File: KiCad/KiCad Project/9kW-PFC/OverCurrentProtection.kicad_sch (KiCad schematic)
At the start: 0 parts

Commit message: Added submodule for KiCad Library
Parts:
- added U1: MCP6004, Package_SO:SOIC-14_3.9x8.7mm_P1.27mm, symbol Amplifier_Operational:MCP6004

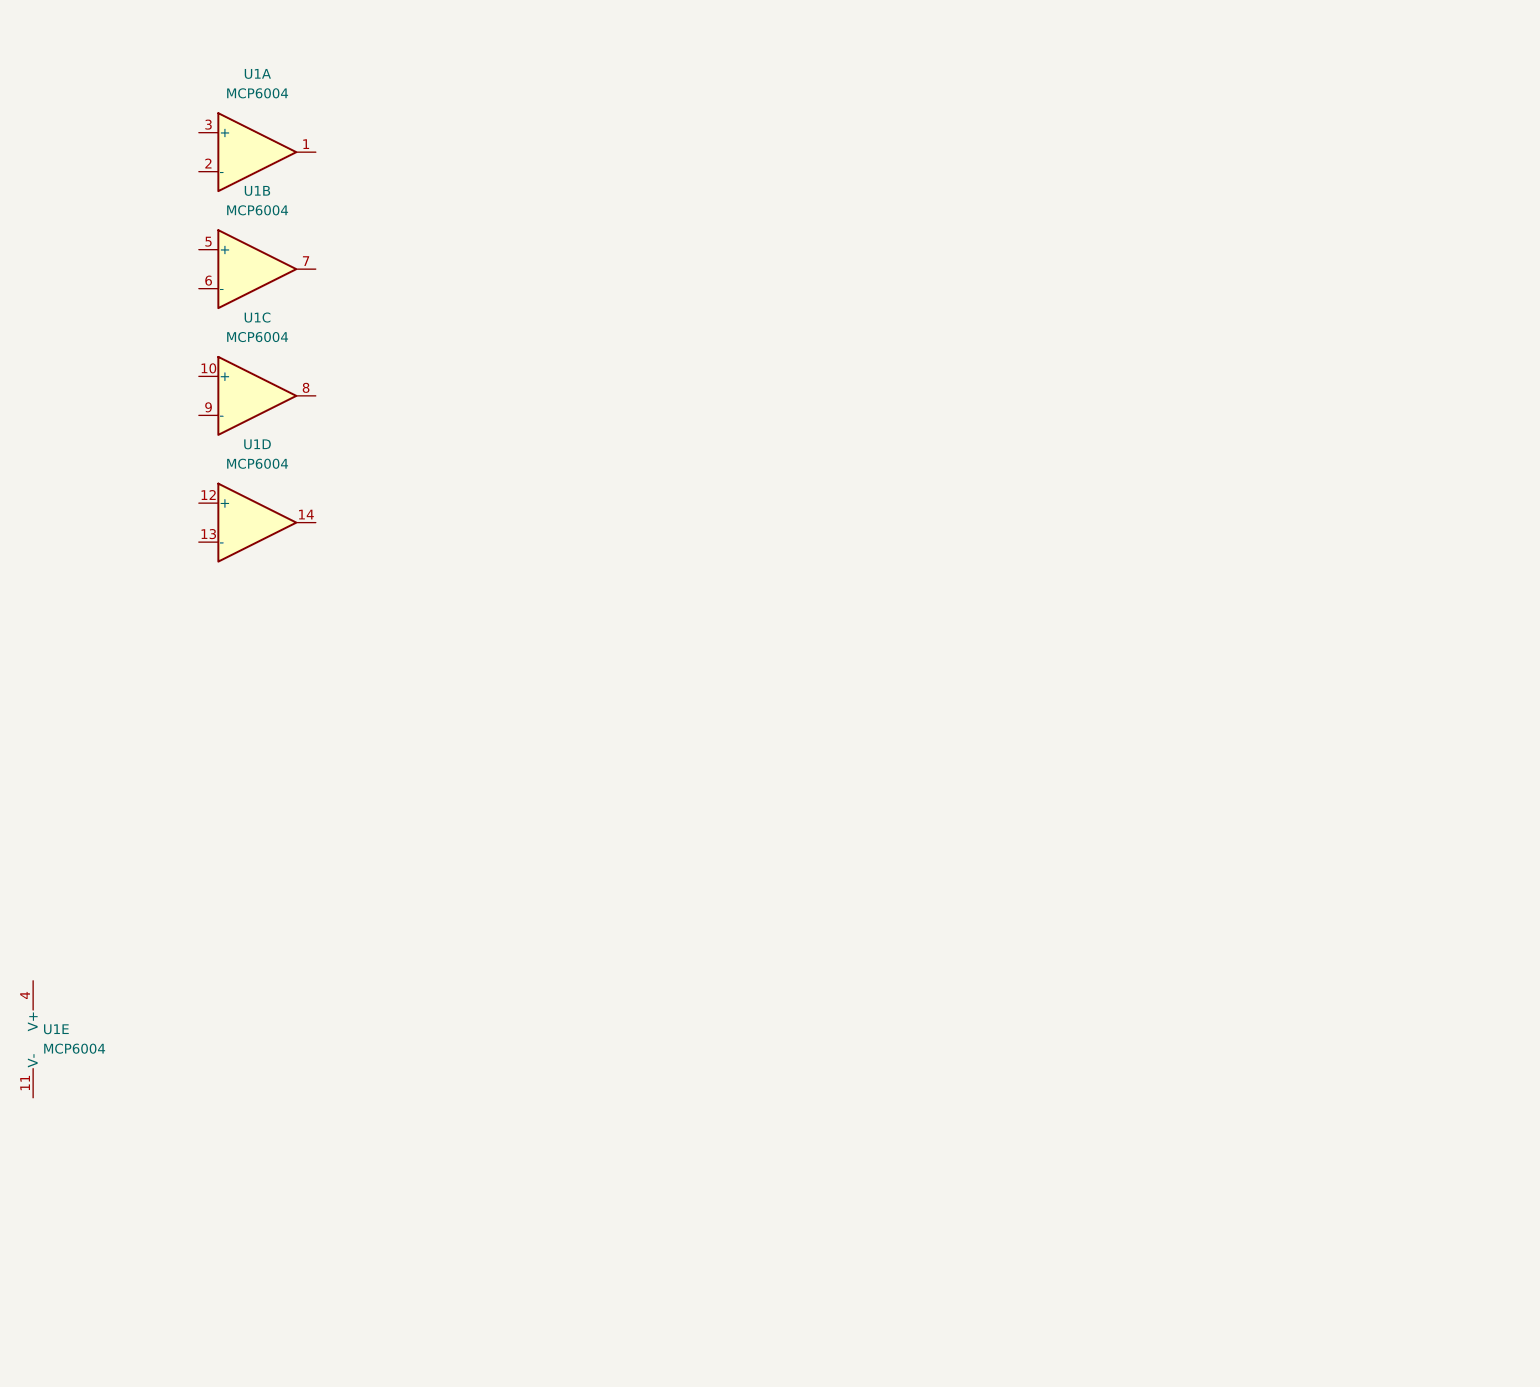
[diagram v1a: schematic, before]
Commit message: Started on Over Current Protection
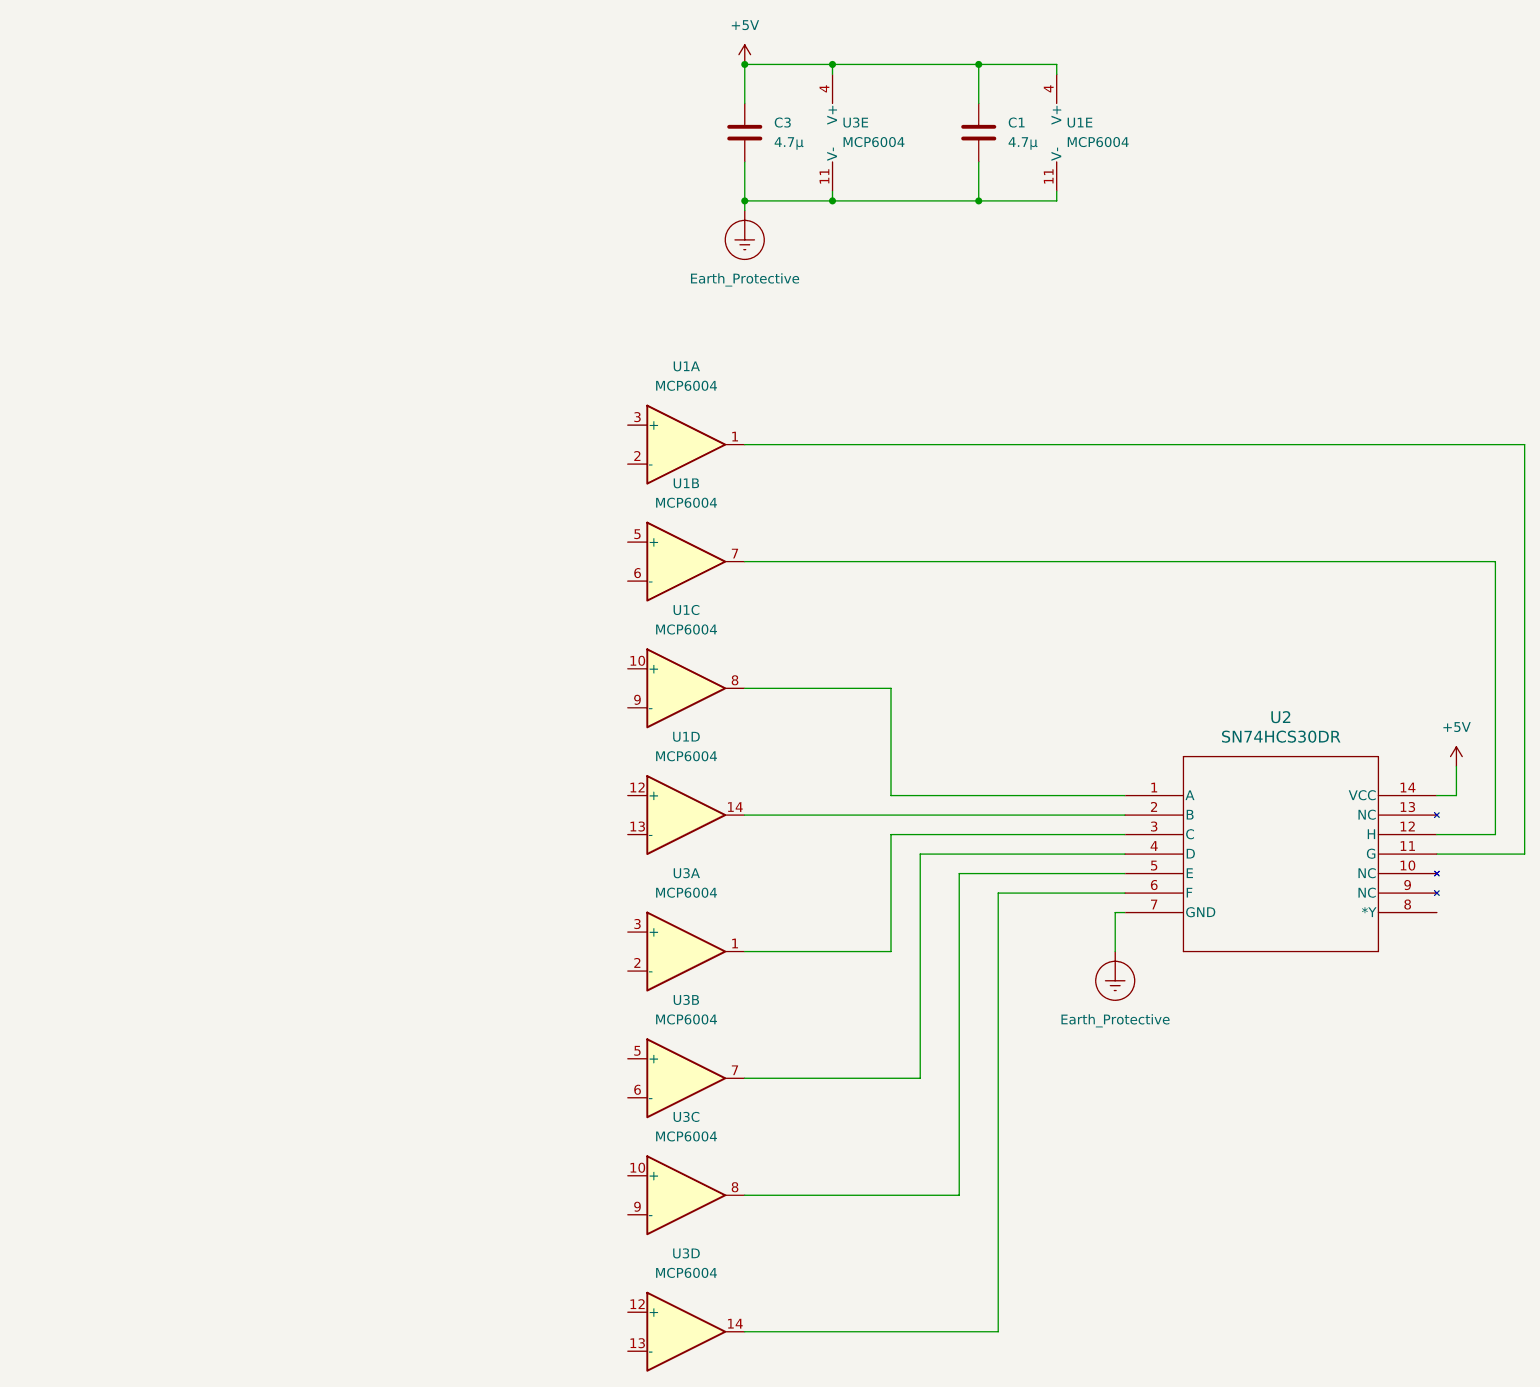
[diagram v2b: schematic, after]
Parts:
- added C1, C3: 4.7µ, Capacitor_SMD:C_0805_2012Metric_Pad1.18x1.45mm_HandSolder, symbol Device:C
- added U2: SN74HCS30DR, SN74S133DR:SOIC14-D_TEX, symbol NAND Gate 8-input 1-output:SN74HCS30DR
- added U3: MCP6004, symbol Amplifier_Operational:MCP6004
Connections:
- net at U1.1: now also U2.11 (G)
- net at U1.8: now also U2.1 (A)
- net Earth_Protective: now reaches U1.11 (V-)
- net Earth_Protective: now also C1.2, C3.2, U2.7 (GND), U3.11 (V-)
- net +5V: now reaches U1.4 (V+)
- net +5V: now also C1.1, C3.1, U2.14 (VCC), U3.4 (V+)
- net at U1.7: now also U2.12 (H)
- net at U1.14: now also U2.2 (B)
- new net: U2.3 (C), U3.1
- new net: U2.4 (D), U3.7
- new net: U2.5 (E), U3.8
- new net: U2.6 (F), U3.14
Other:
- moved on the sheet: U1A, U1B, U1C, U1D, U1E
